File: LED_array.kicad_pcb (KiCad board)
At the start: 4 copper layers, 40 x 40 mm, 129 parts, among them J1 5040500691

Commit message: finalized LED
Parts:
- moved J1 61.1 mm to (64.0, 30.9)
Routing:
- net GND: track 282.1 -> 94.2 mm, vias 76 -> 79
- net +5VD: track 256.0 -> 103.9 mm, vias 64 -> 65
- net /SDI: track 0.00 -> 16.8 mm
- net /CKI: track 0.01 -> 15.3 mm
- net Net-(D16-Pad2): track 22.7 -> 8.97 mm
- net Net-(D112-Pad2): track 22.6 -> 9.89 mm
- net Net-(D112-Pad3): track 6.00 -> 7.56 mm
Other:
- board size 40 x 40 mm -> 40 x 48 mm

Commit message: Adding in resistors and capacitor pads
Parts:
- added 5V: SolderWirePad_1x01_SMD_1x2mm, Connector_Wire:SolderWirePad_1x01_SMD_1x2mm, B.Cu at (54.8, 47.5)
- added Gnd: SolderWirePad_1x01_SMD_1x2mm, Connector_Wire:SolderWirePad_1x01_SMD_1x2mm, B.Cu at (65.2, 47.3)
- added R1: 68R, Resistor_SMD:R_0603_1608Metric, F.Cu at (58.4, 32.6)
- added R2: 68R, Resistor_SMD:R_0603_1608Metric, F.Cu at (62.6, 32.6)
- moved J1 1.15 mm to (64.1, 29.7)
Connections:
- J1 pad 2: /SDI -> Net-(J1-Pad2)
- J1 pad 4: /CKI -> Net-(J1-Pad4)
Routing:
- net GND: track 94.2 -> 99.4 mm
- net /CKI: track 15.3 -> 10.9 mm
- net /SDI: track 16.8 -> 12.9 mm
- net Net-(J1-Pad2): track 0.00 -> 3.18 mm
- net Net-(J1-Pad4): track 0.00 -> 2.98 mm
- net +5VD: track 103.9 -> 105.2 mm

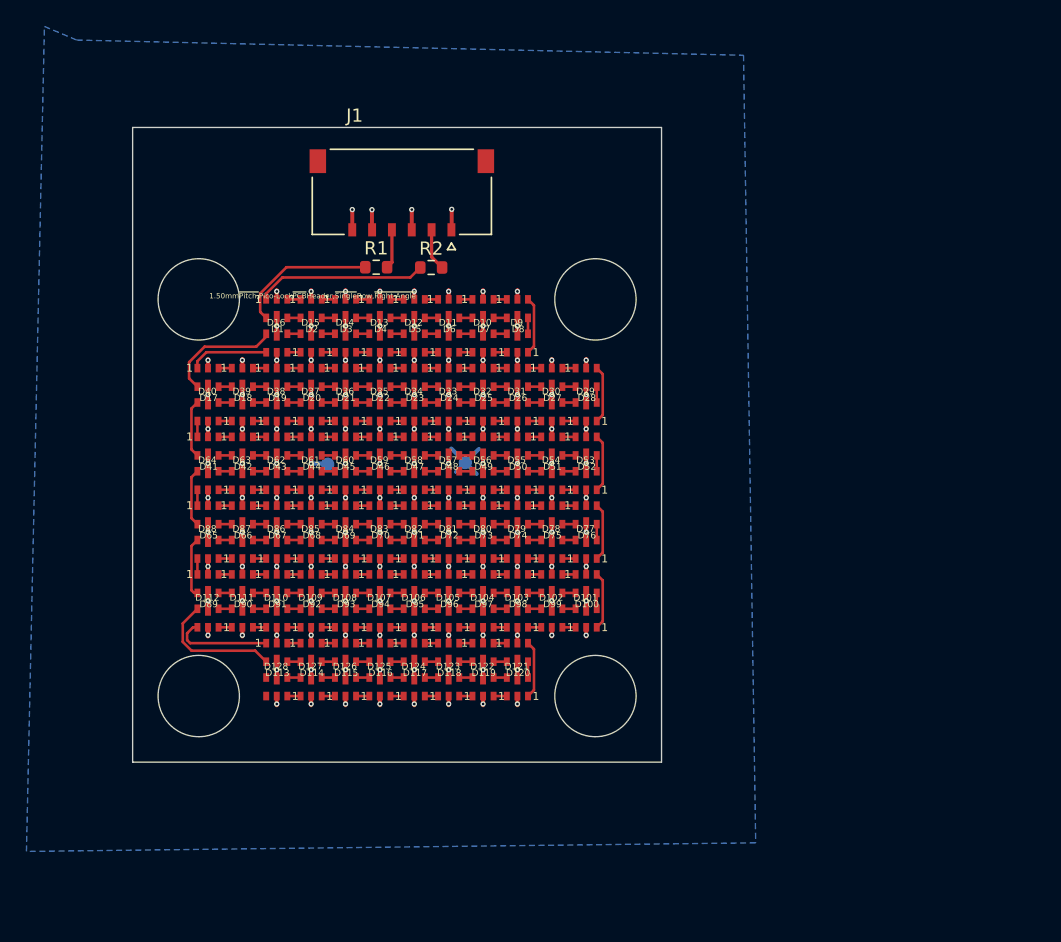
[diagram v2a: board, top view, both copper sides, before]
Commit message: minor edits + generation of fab files edits: (1) add capacitors (2) change via and track size for the picolock conenctor (3) update the picolock connector footprint for handsoldering (4) remove label D1-D128 and the 1s (5) change corner to round (6) add text notes for the board
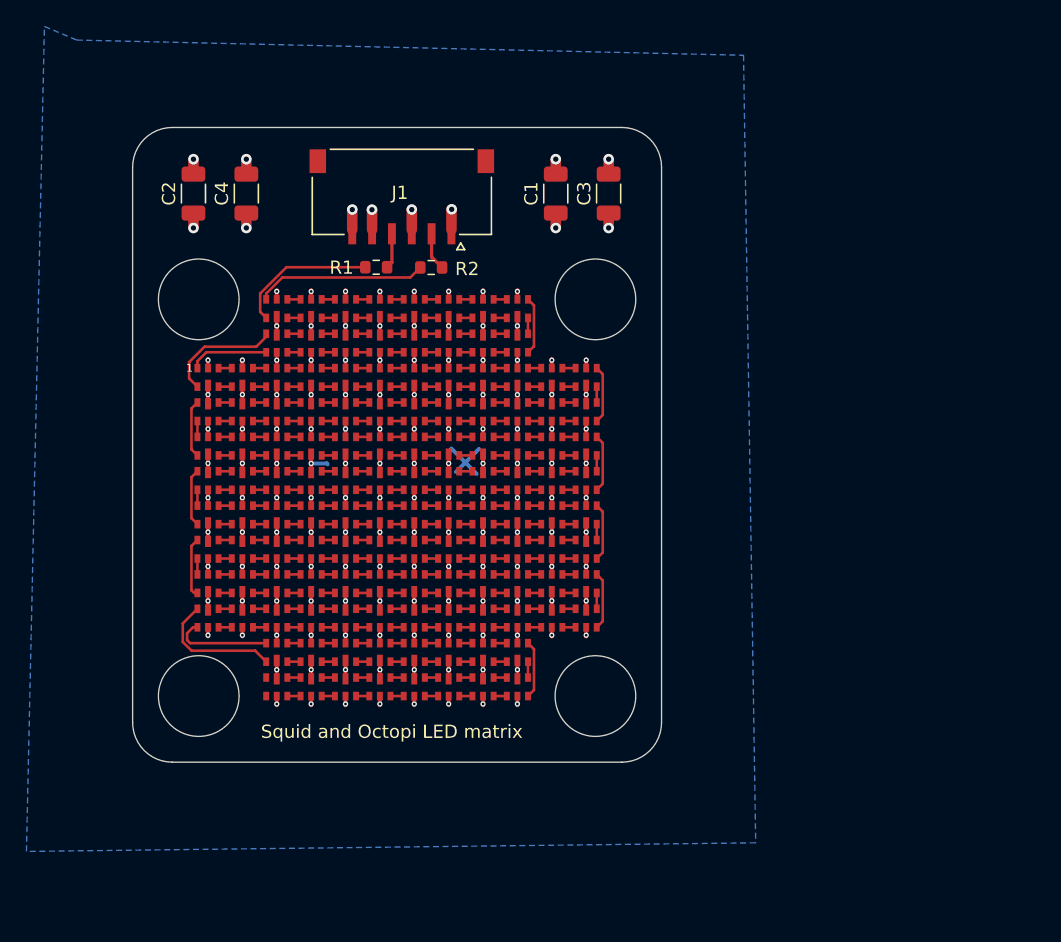
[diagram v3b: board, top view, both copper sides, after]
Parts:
- removed 5V, Gnd: SolderWirePad_1x01_SMD_1x2mm, Connector_Wire:SolderWirePad_1x01_SMD_1x2mm
- added C1: 4.7u, Capacitor_SMD:C_1206_3216Metric, F.Cu at (72.0, 27.0)
- added C2: 4.7u, Capacitor_SMD:C_1206_3216Metric, F.Cu at (44.6, 27.0)
- added C3: 4.7u, Capacitor_SMD:C_1206_3216Metric, F.Cu at (76.0, 27.0)
- added C4: 4.7u, Capacitor_SMD:C_1206_3216Metric, F.Cu at (48.6, 27.0)
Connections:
- D128 pad 2: Net-(D128-Pad2) -> (no net)
- D128 pad 3: Net-(D128-Pad3) -> (no net)
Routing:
- net GND: track 99.4 -> 103.9 mm, vias 79 -> 83
- net +5VD: track 105.2 -> 109.7 mm, vias 65 -> 69
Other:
- outline, holes or cut-outs redrawn
- board text added: "Designed by Rinni Bhansali With minor edits from Hongquan Li Prakash Lab, Stanford University 04/12/2021"
- board text added: "Squid and Octopi LED matrix"
